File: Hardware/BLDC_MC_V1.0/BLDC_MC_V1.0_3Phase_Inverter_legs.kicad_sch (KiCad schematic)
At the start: 6 parts, among them Q1 BSC0702LS, Q2 BSC0702LS, Q3 BSC0702LS, Q4 BSC0702LS, Q5 BSC0702LS, Q6 BSC0702LS

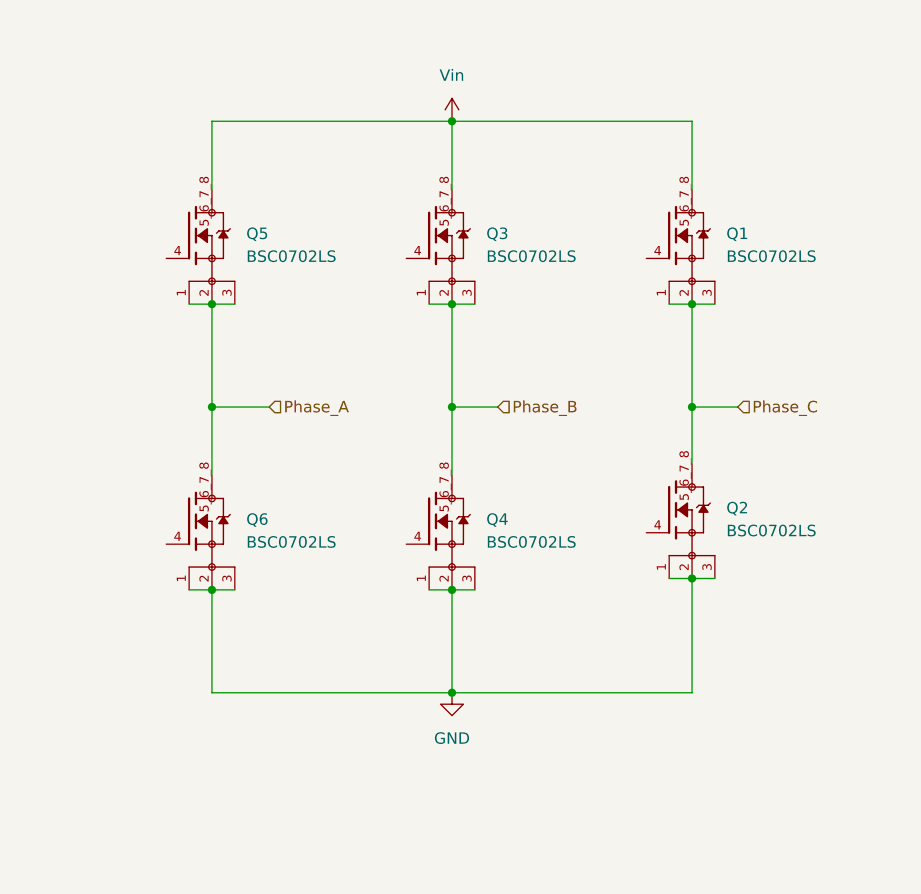
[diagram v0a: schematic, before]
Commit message: Edit the connection between sheets and add some details and connections to gatedrive sheet
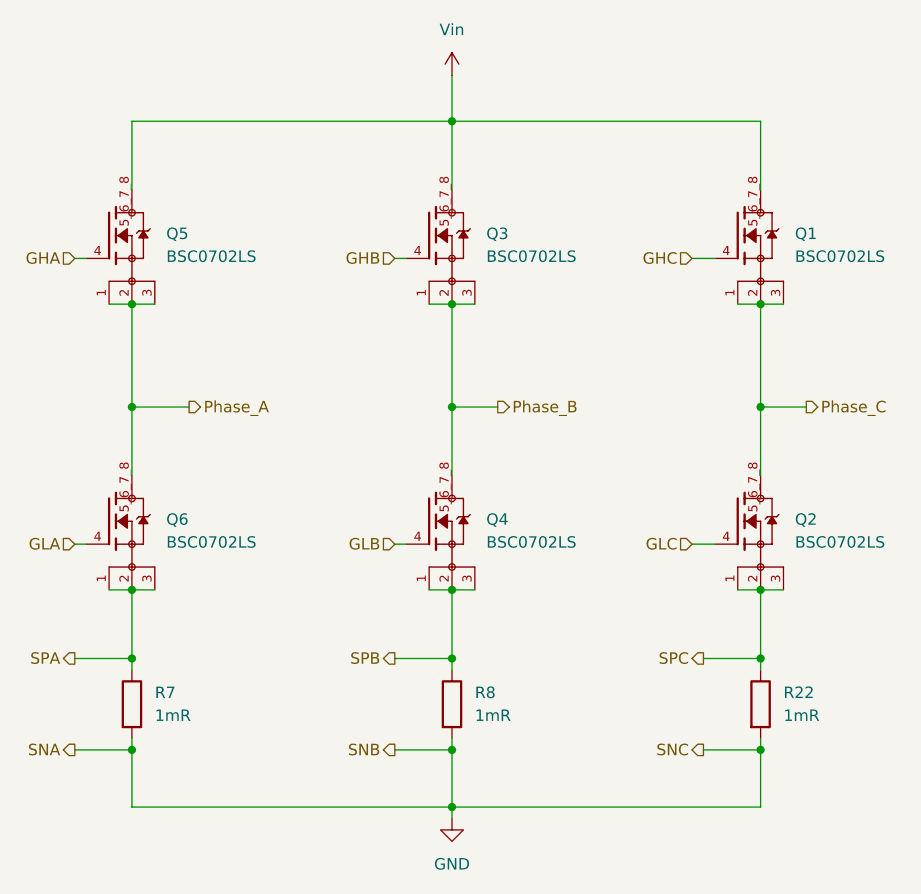
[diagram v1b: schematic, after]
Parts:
- added R22, R7, R8: 1mR, Resistor_SMD:R_2512_6332Metric, symbol Device:R
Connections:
- net GND: now also R22.2, R7.2, R8.2; no longer Q2.1, Q2.2, Q2.3, Q4.1, Q4.2, Q4.3, Q6.1, Q6.2, Q6.3
- net GHC: now reaches Q1.4
- net GHA: now reaches Q5.4
- net GHB: now reaches Q3.4
- net GLB: now reaches Q4.4
- net GLA: now reaches Q6.4
- net GLC: now reaches Q2.4
- new net SPA: Q6.1, Q6.2, Q6.3, R7.1
- new net SPB: Q4.1, Q4.2, Q4.3, R8.1
- new net SPC: Q2.1, Q2.2, Q2.3, R22.1
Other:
- moved on the sheet: Q1, Q2, Q5, Q6

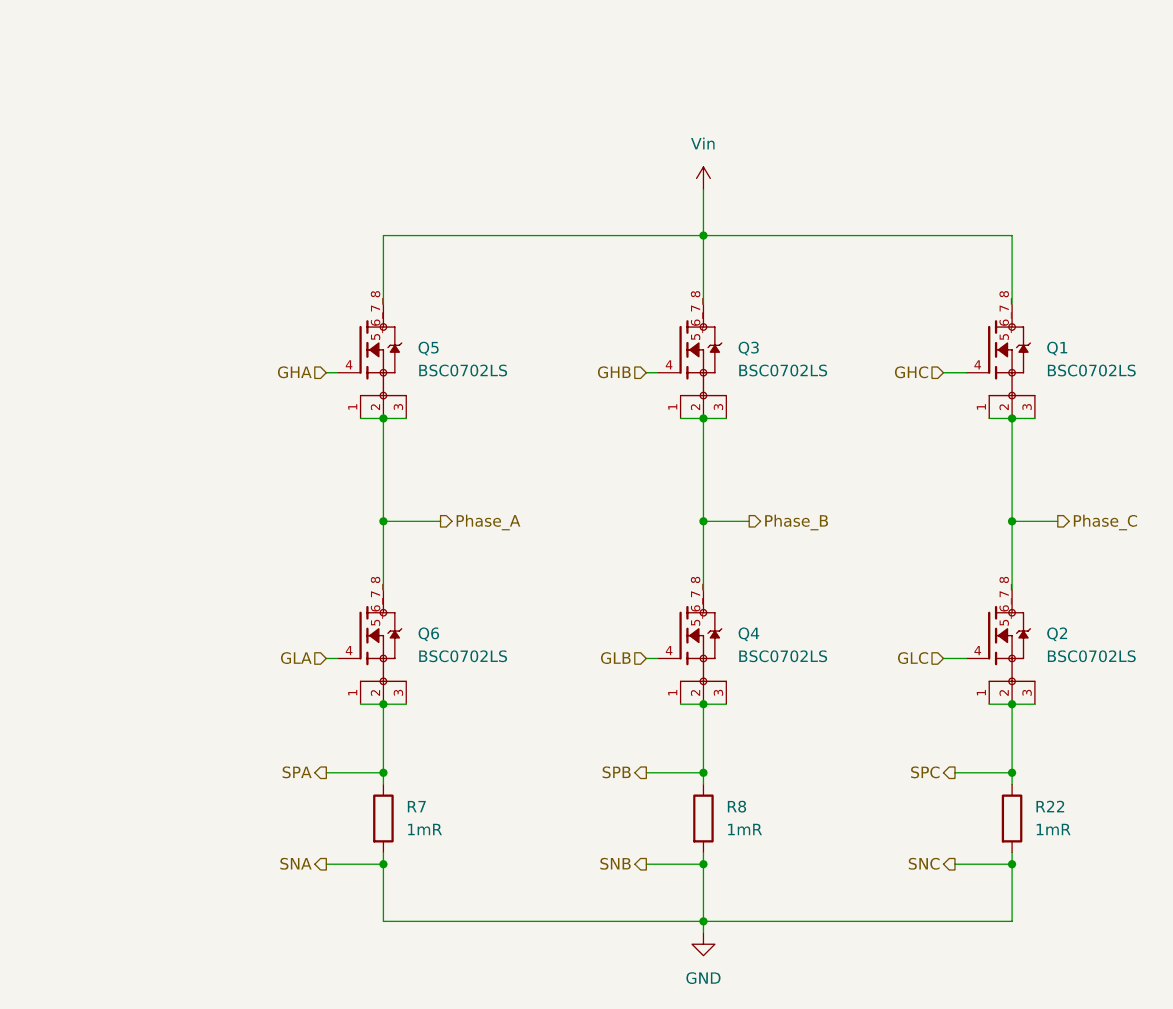
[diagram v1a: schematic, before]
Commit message: Restore the importenat project files from last commit and define the routing of current sensor as differntial pair
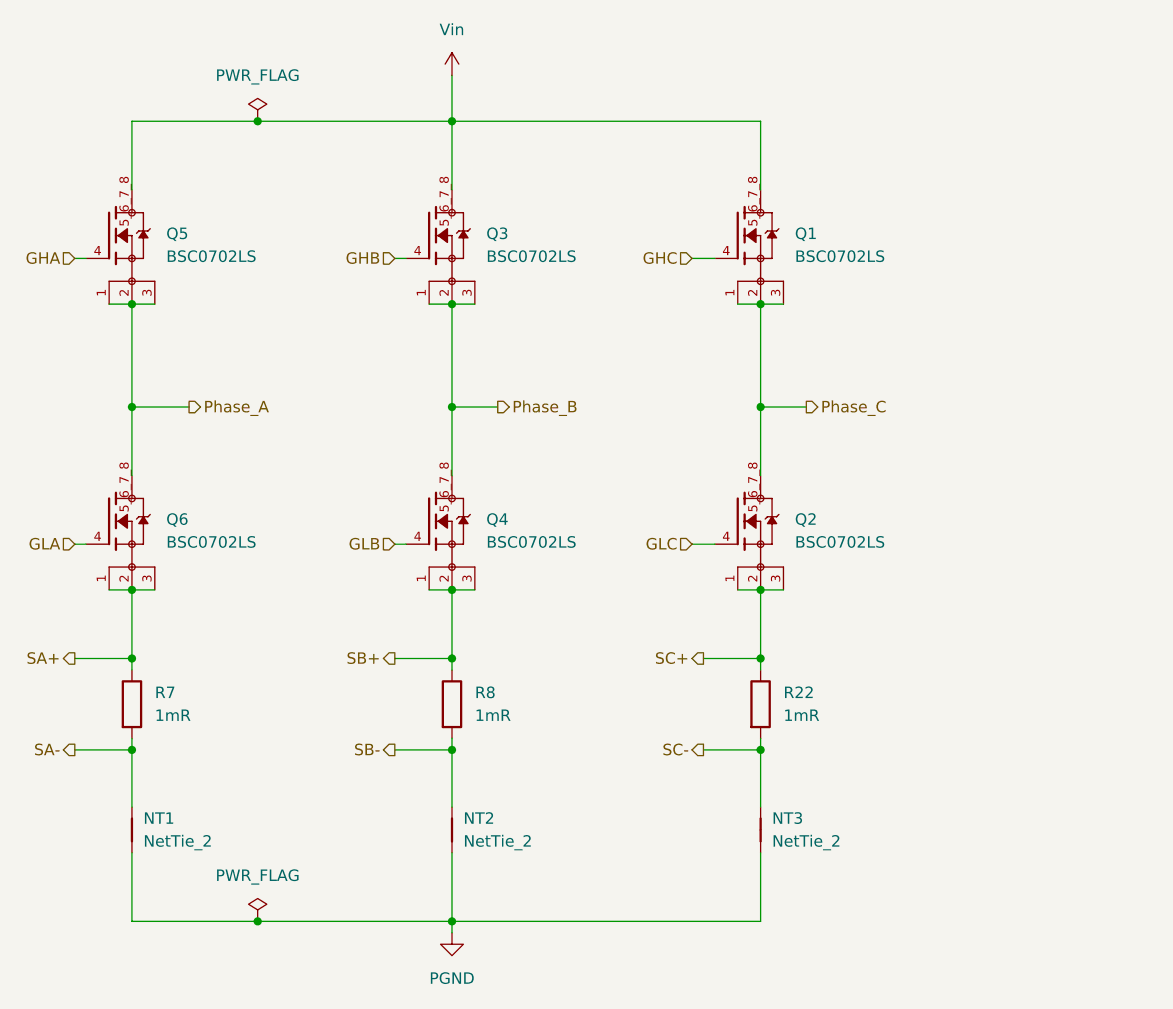
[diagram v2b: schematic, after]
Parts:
- added NT1, NT2, NT3: NetTie_2, NetTie:NetTie-2_SMD_Pad2.0mm, symbol Device:NetTie_2
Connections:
- removed net GND: R22.2, R7.2, R8.2
- net SPA renamed SA+
- net SPB renamed SB+
- net SPC renamed SC+
- new net PGND: NT1.1, NT2.1, NT3.1
- new net SA-: NT1.2, R7.2
- new net SB-: NT2.2, R8.2
- new net SC-: NT3.2, R22.2
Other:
- moved on the sheet: Q1, Q2, Q3, Q4, Q5, Q6, R22, R7, R8

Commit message: Edit project confg
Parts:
- added C45, C46: 100nF, Capacitor_SMD:C_0805_2012Metric, symbol Device:C
- added C47, C48, C49, C50: 47uF, Capacitor_SMD:CP_Elec_10x10.5, symbol Device:C_Polarized
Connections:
- net Vin: now also C45.1, C46.1, C47.1, C48.1, C49.1, C50.1
- new net GND: C45.2, C46.2, C47.2, C48.2, C49.2, C50.2
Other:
- moved on the sheet: NT1, NT2, NT3, Q1, Q2, Q3, Q4, Q5, Q6, R22, R7, R8

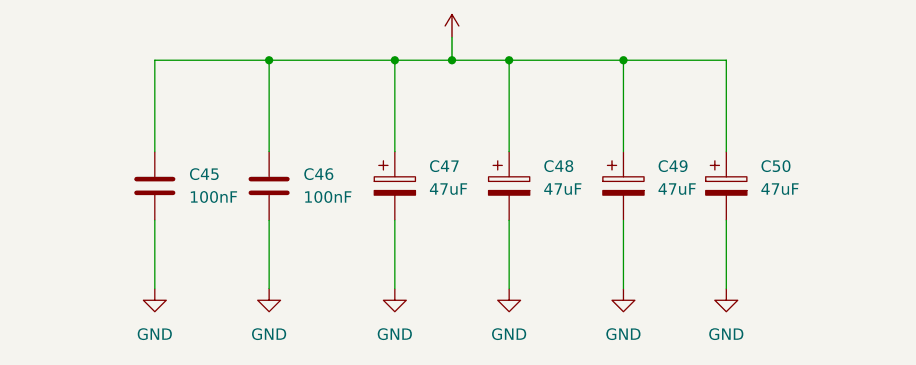
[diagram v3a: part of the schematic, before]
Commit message: Edit the ground of the capacitors to PGND
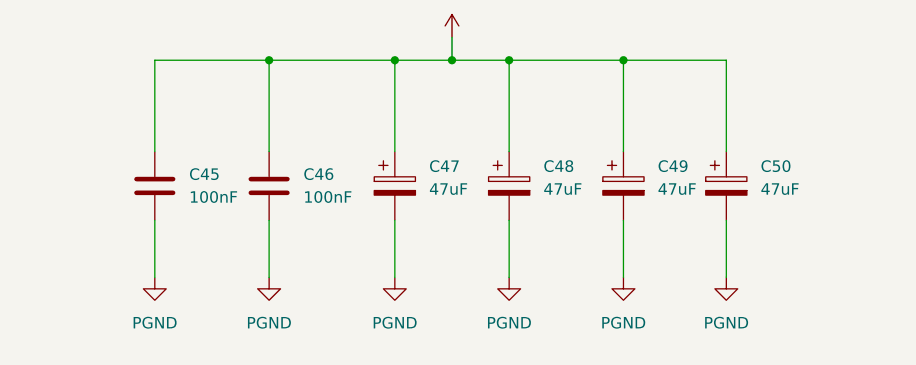
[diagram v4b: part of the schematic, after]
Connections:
- net GND is gone; now on net PGND: C45.2, C46.2, C47.2, C48.2, C49.2, C50.2

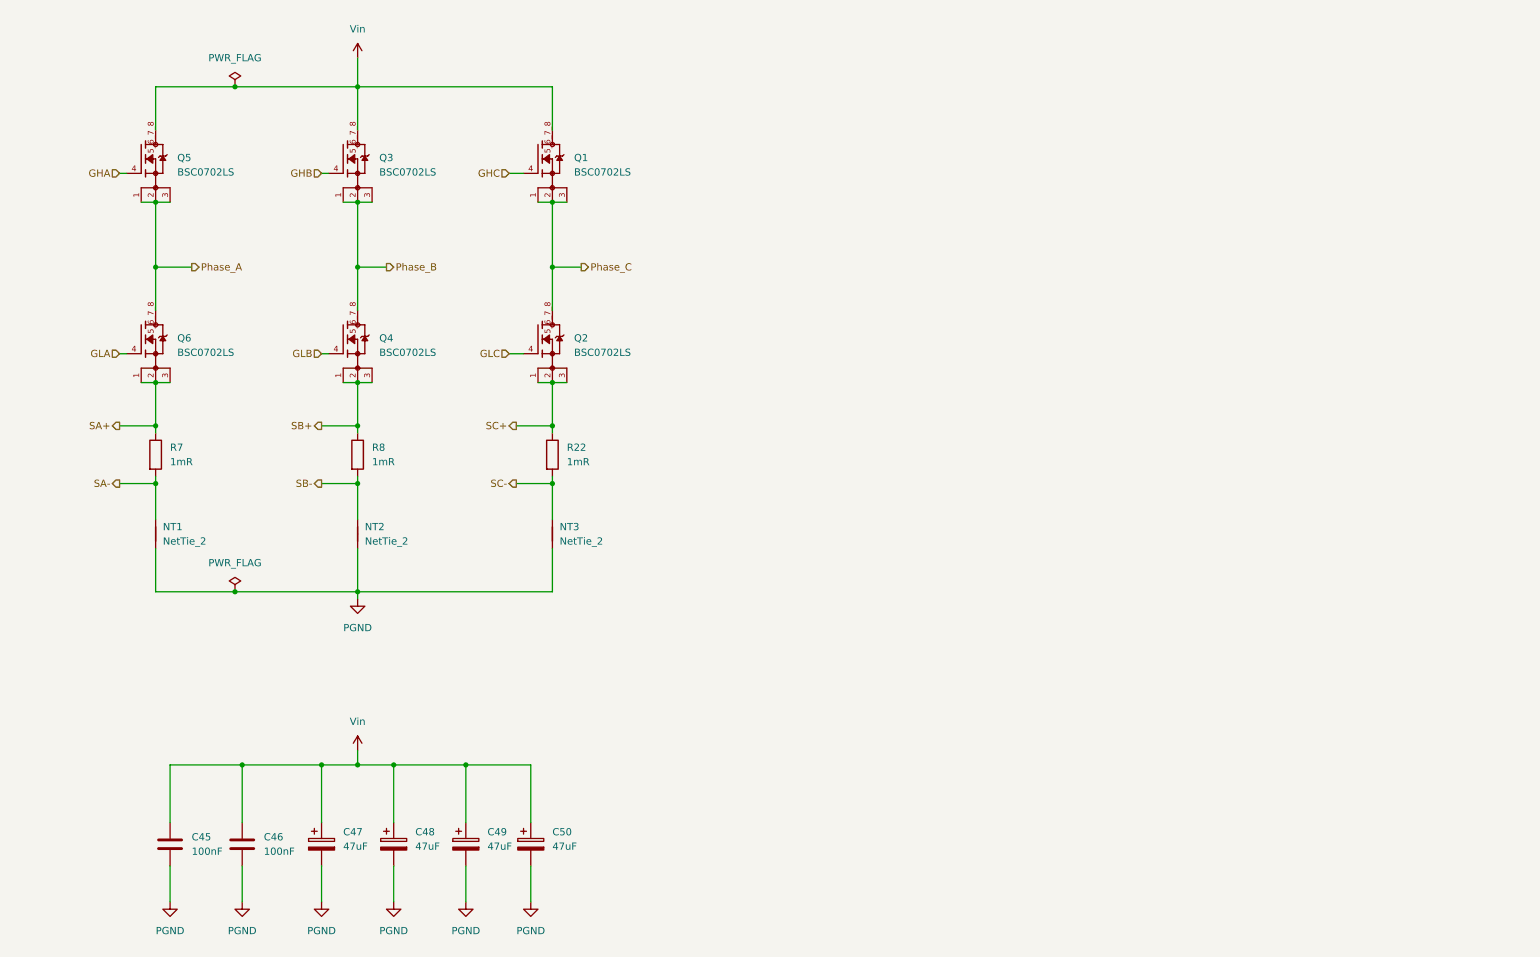
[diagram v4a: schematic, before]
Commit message: Add the snubber circuit and arrange the sheet
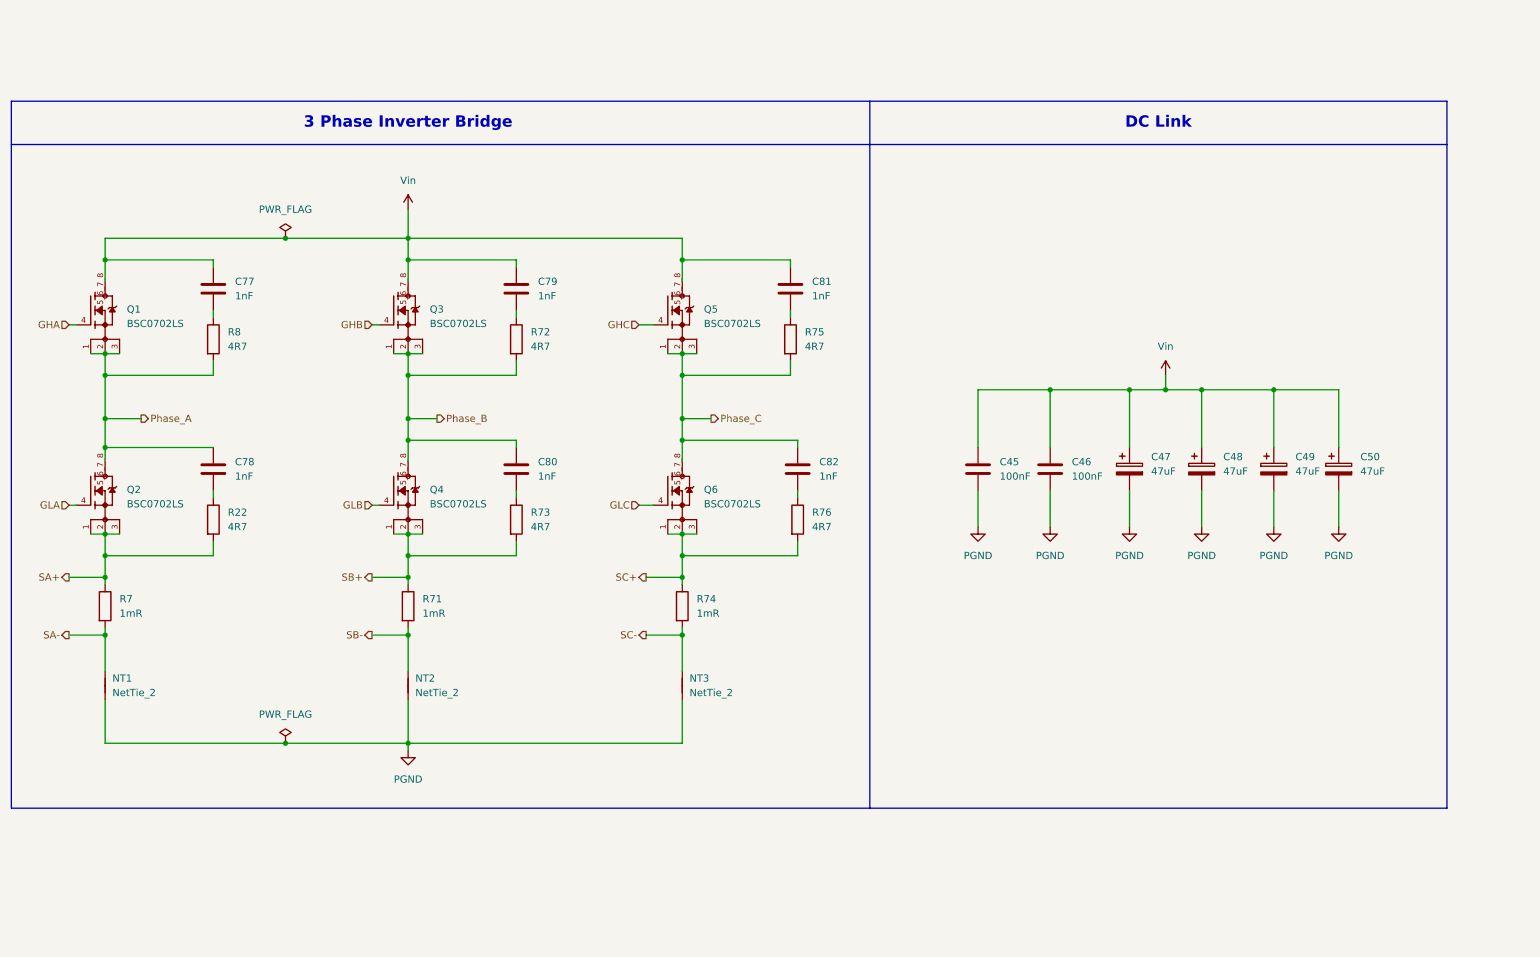
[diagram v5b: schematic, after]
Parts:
- added C77, C78, C79, C80, C81, C82: 1nF, Capacitor_SMD:C_1206_3216Metric, symbol Device:C
- added R22, R72, R73, R75, R76, R8: 4R7, Resistor_SMD:R_2512_6332Metric_Pad1.40x3.35mm_HandSolder, symbol Device:R
- renumbered Q5 to Q1, Q6 to Q2, Q1 to Q5, Q2 to Q6, R8 to R71, R22 to R74
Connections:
- net Phase_A: now also C78.1, R8.2
- net Phase_B: now also C80.1, R72.2
- net Phase_C: now also C82.1, R75.2
- net SA+: now also R22.2
- net SB+: now also R73.2
- net SC+: now also R76.2
- net Vin: now also C77.1, C79.1, C81.1
- new net: C82.2, R76.1
- new net: C81.2, R75.1
- new net: C77.2, R8.1
- new net: C79.2, R72.1
- new net: C78.2, R22.1
- new net: C80.2, R73.1
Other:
- note added: "3 Phase Inverter Bridge"
- note added: "DC Link"
- moved on the sheet: C45, C46, C47, C48, C49, C50, NT1, NT2, NT3, Q1, Q2, Q3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

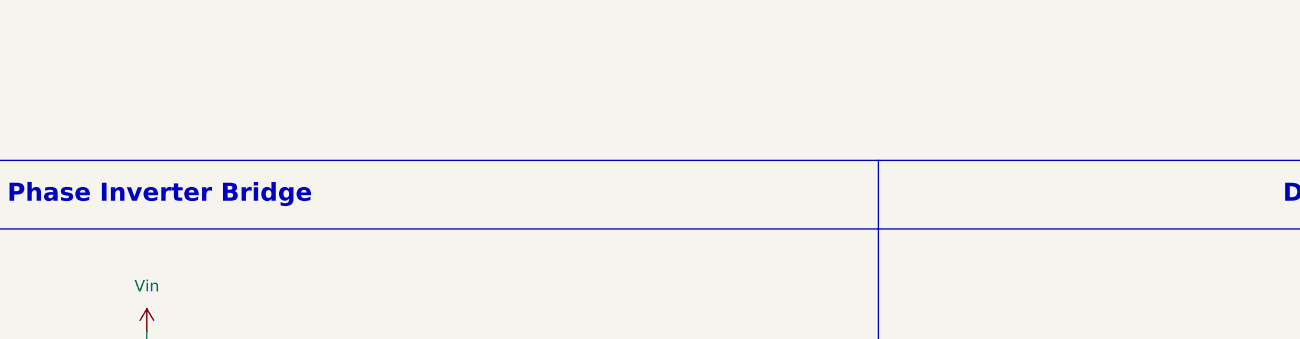
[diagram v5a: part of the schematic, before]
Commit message: Adjust the connections between sheets
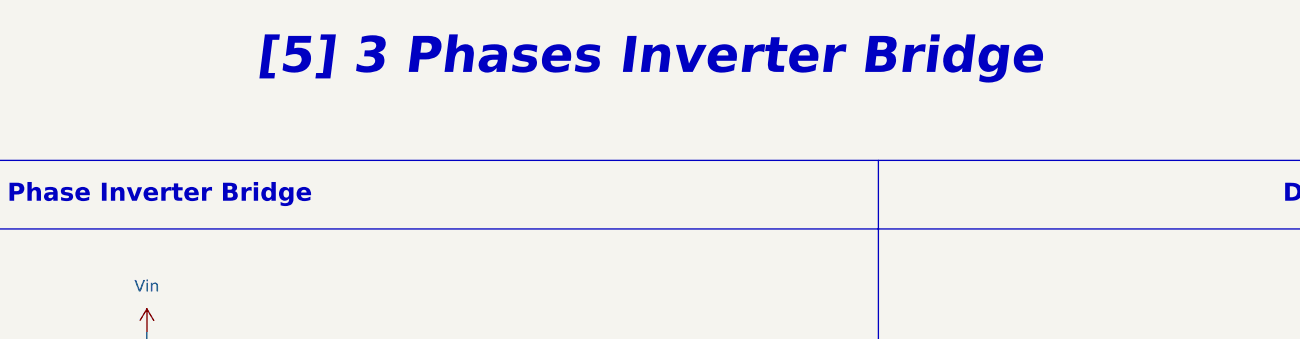
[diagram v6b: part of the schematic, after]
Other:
- note added: "[5] 3 Phases Inverter Bridge"
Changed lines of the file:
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@@
+		)
+	)
+	(text "[5] 3 Phases Inverter Bridge\n"
+		(exclude_from_sim no)
+		(at 146.05 27.94 0)
+		(effects
+			(font
+				(size 4 4)
+				(thickness 0.8)
+				(bold yes)
+				(italic yes)
+				(color 132 0 0 1)
+			)
 		)
 	)

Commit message: Solve all errors and wornings in project
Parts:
- removed Q1, Q2, Q3, Q4, Q5, Q6: BSC0702LS, BLDC_Motor_Driver_Components_Footprint:TRANS_BSC0702LS, symbol BSC0702LS:BSC0702LS
- added Q1, Q2, Q3, Q4, Q5, Q6: BSC027N10NS5ATMA1, BLDC_Motor_Driver_Components_Footprint:PG-TSON-8-3_INF, symbol BSC027N10NS5ATMA1:BSC027N10NS5ATMA1
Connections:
- net GHA: now also Q1.4
- net GHB: now also Q2.4
- net GHC: now also Q3.4
- net GLA: now also Q6.4
- net GLB: now also Q5.4
- net GLC: now also Q4.4
- net Phase_A: now also Q1.1, Q1.2, Q1.3, Q6.5, Q6.6, Q6.7, Q6.8
- net Phase_B: now also Q2.1, Q2.2, Q2.3, Q5.5, Q5.6, Q5.7, Q5.8
- net Phase_C: now also Q3.1, Q3.2, Q3.3, Q4.5, Q4.6, Q4.7, Q4.8
- net SA+: now also Q6.1, Q6.2, Q6.3
- net SB+: now also Q5.1, Q5.2, Q5.3
- net SC+: now also Q4.1, Q4.2, Q4.3
- net Vin: now also Q1.5, Q1.6, Q1.7, Q1.8, Q2.5, Q2.6, Q2.7, Q2.8, Q3.5, Q3.6, Q3.7, Q3.8
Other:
- moved on the sheet: C77, C78, C79, C80, C81, C82, R22, R72, R73, R75, R76, R8
